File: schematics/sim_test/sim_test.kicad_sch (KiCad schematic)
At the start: 6 parts, among them U1 INA849D

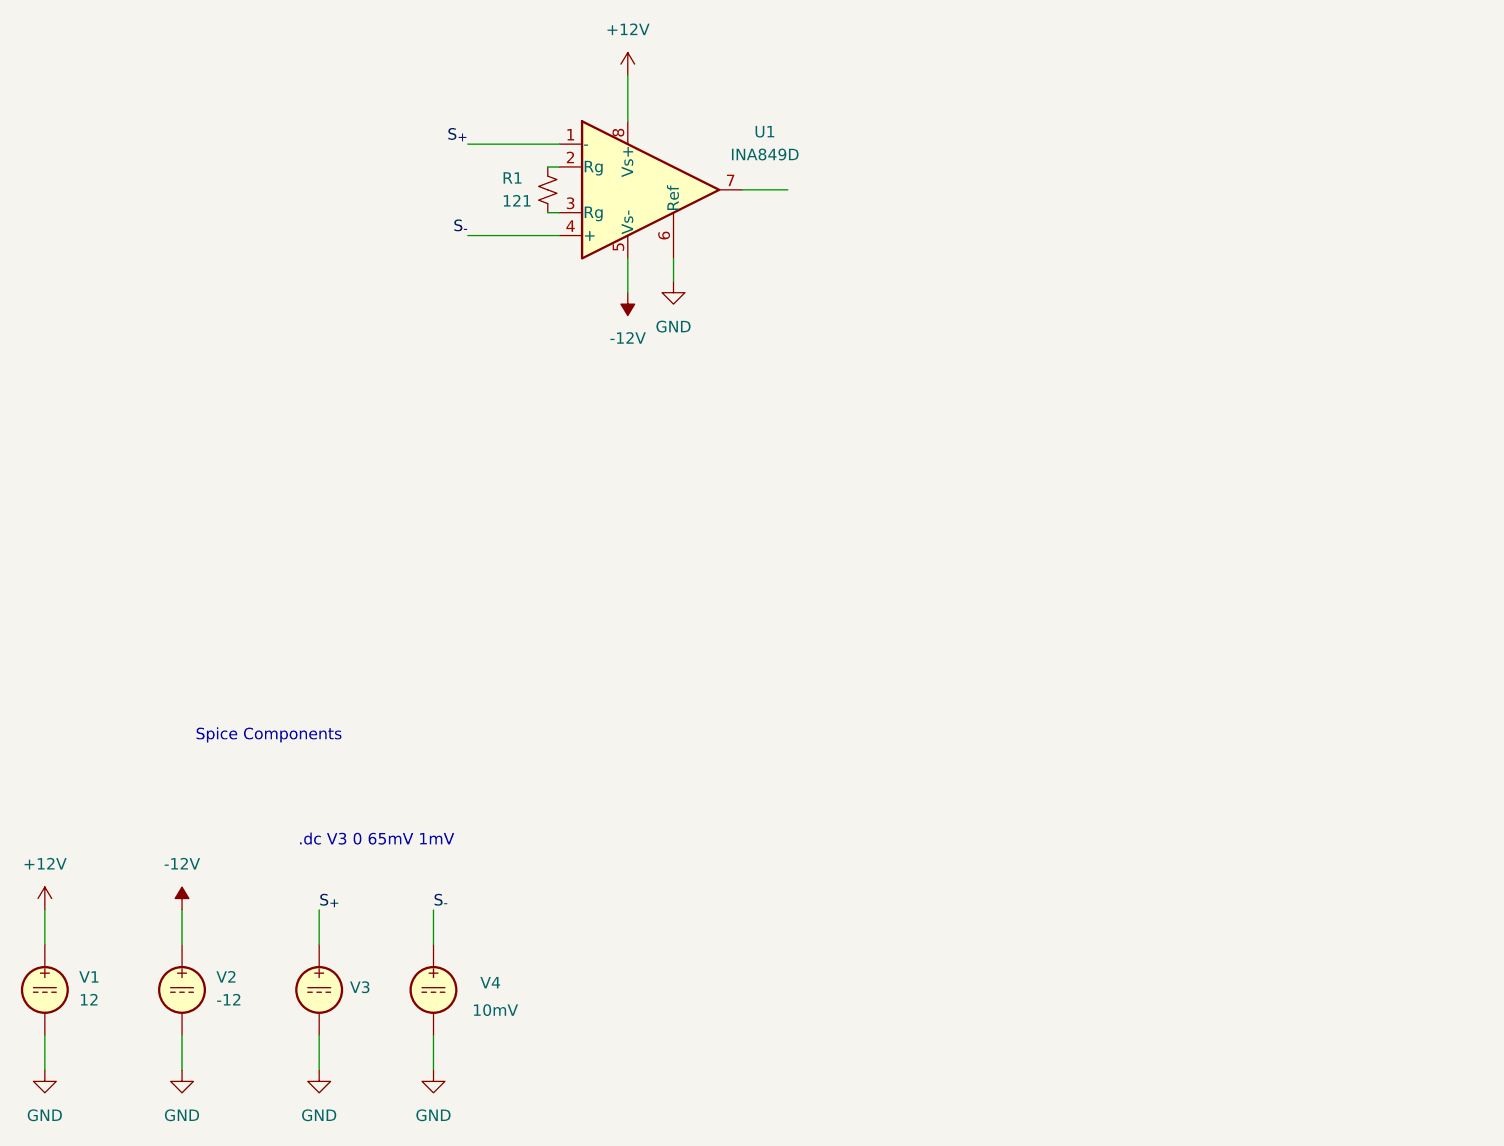
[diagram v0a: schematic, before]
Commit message: feat(sim): SG sig chain
Signed-off-by: Andrew Balmos <andrew@balmos.org>
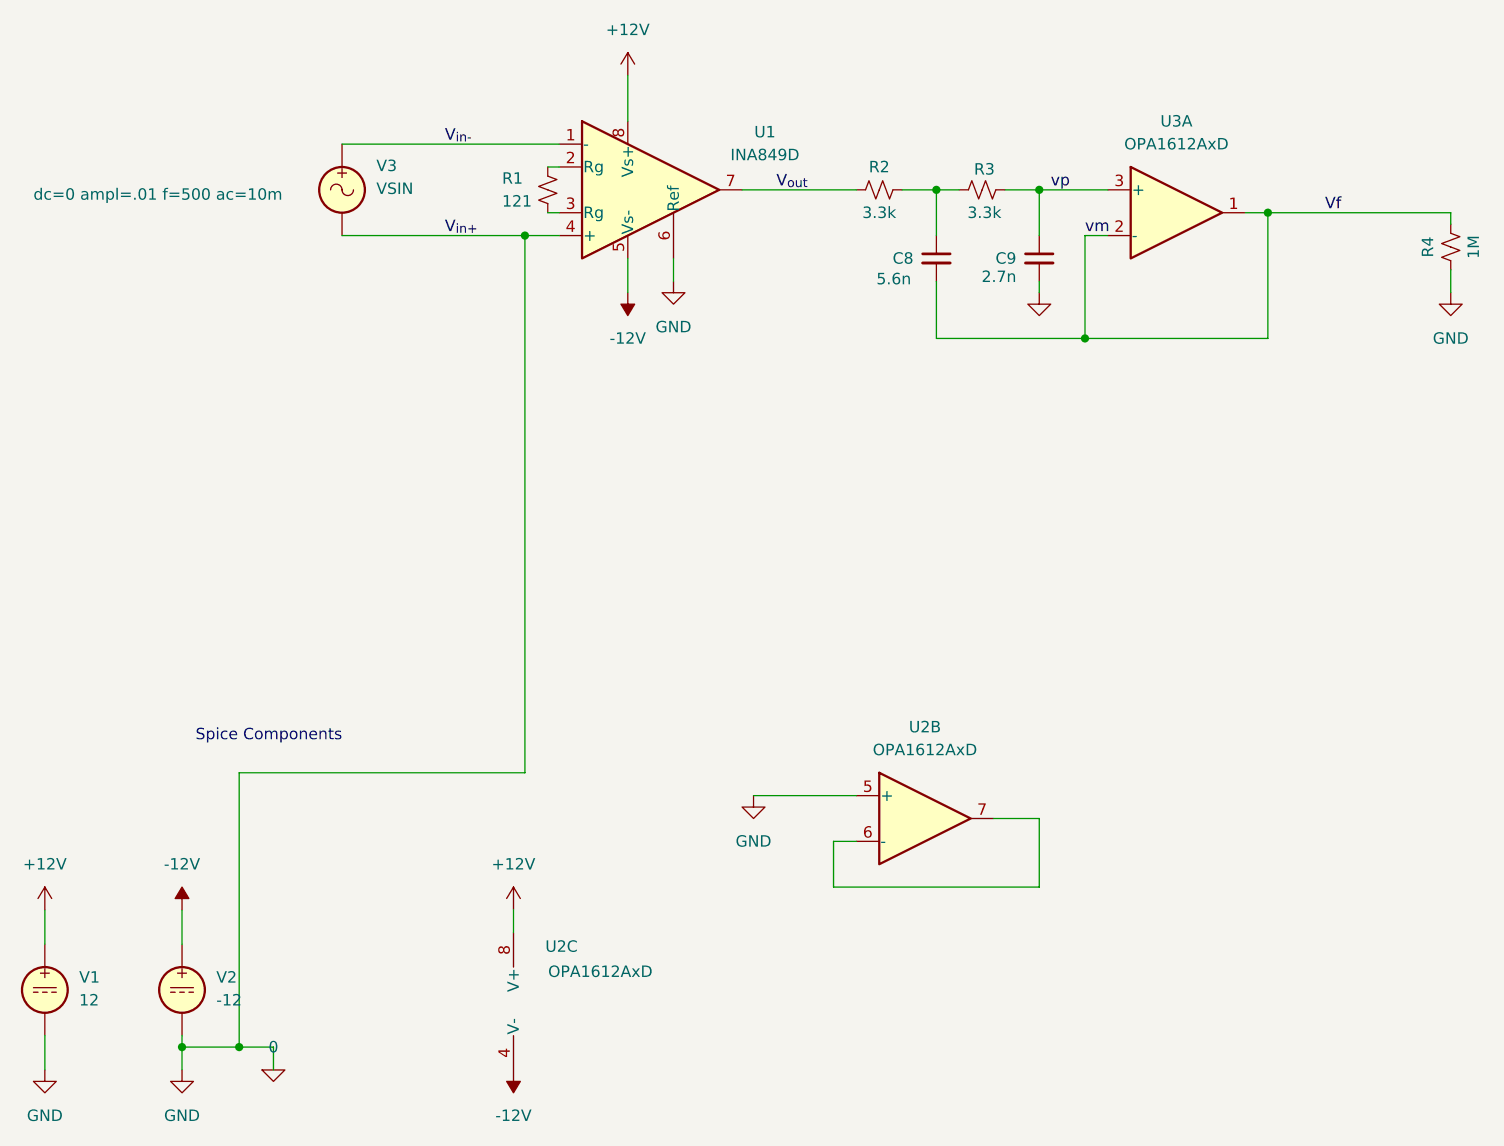
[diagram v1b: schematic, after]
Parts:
- removed V3: 1, symbol Simulation_SPICE:VDC
- removed V4: 10mV, symbol Simulation_SPICE:VDC
- added C8: 5.6n, Capacitor_SMD:C_0402_1005Metric, symbol Device:C_Small
- added C9: 2.7n, Capacitor_SMD:C_0402_1005Metric, symbol Device:C_Small
- added R2, R3: 3.3k, Resistor_SMD:R_0603_1608Metric, symbol Device:R_Small_US
- added R4: 1M, Resistor_SMD:R_0603_1608Metric, symbol Device:R_Small_US
- added U2, U3: OPA1612AxD, Link_Footprints:OPA1612, symbol Amplifier_Operational:OPA1612AxD
- added V3: VSIN, symbol Simulation_SPICE:VSIN
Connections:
- net S_{-} is gone; now on net 0: U1.4 (+)
- net +12V: now also U2.8 (V+)
- net -12V: now also U2.4 (V-)
- net V_{out}: now reaches U1.7
- net V_{out}: now also R2.1
- net GND renamed 0
- net 0: now also C9.2, R4.1, U2.5 (+), V3.2
- net S_{+} renamed V_{in-}
- net V_{in-}: now also V3.1
- new net: C8.1, R2.2, R3.1
- new net: U2.6 (-), U2.7
- new net Vf: C8.2, R4.2, U3.1, U3.2 (-)
- new net vp: C9.1, R3.2, U3.3 (+)
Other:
- note removed: ".dc V3 0 65mV 1mV"

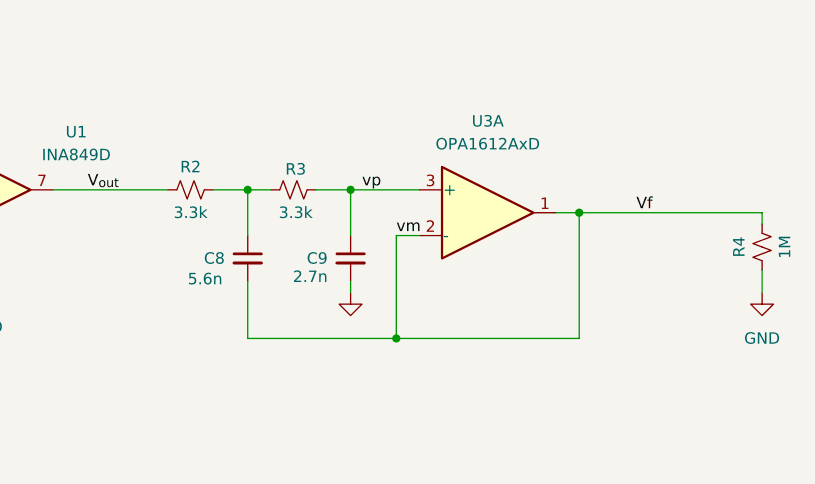
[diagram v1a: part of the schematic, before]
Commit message: bug(sg): Fix sim config
Signed-off-by: Andrew Balmos <andrew@balmos.org>
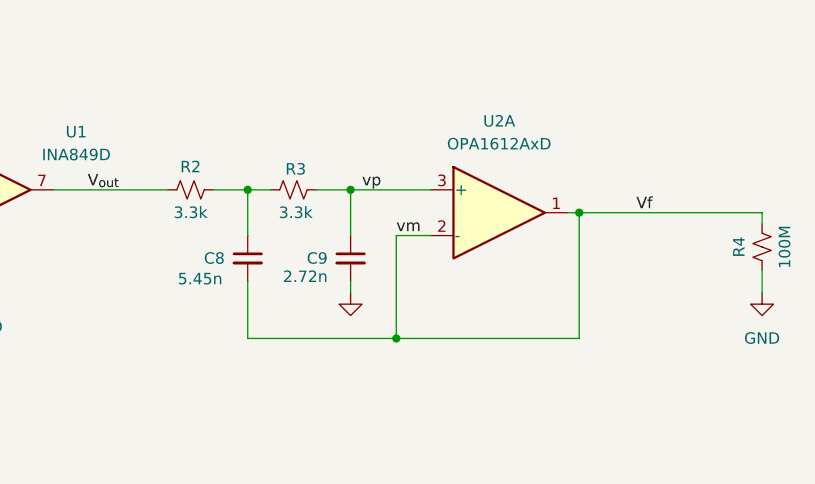
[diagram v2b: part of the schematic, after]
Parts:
- C8: value 5.6n -> 5.45n
- C9: value 2.7n -> 2.72n
- R4: value 1M -> 100M
- renumbered U3 to U2
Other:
- moved on the sheet: U2A

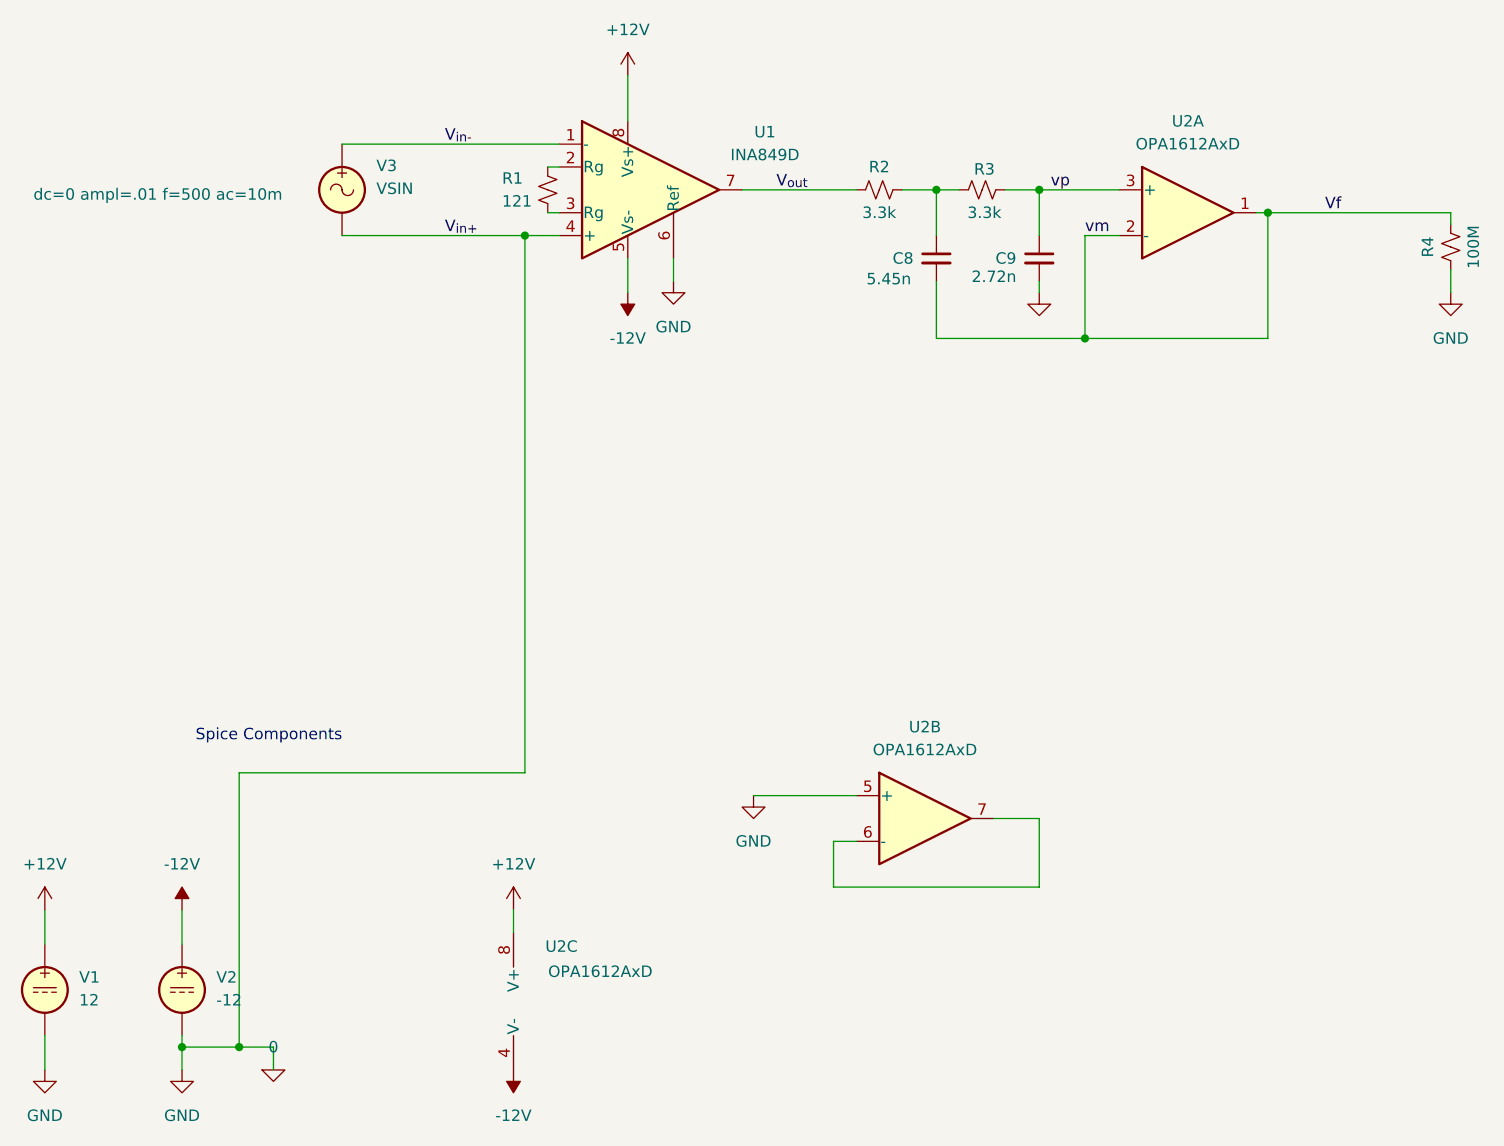
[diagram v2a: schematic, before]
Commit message: bug(sg): remove extra ground wire
Signed-off-by: Andrew Balmos <andrew@balmos.org>
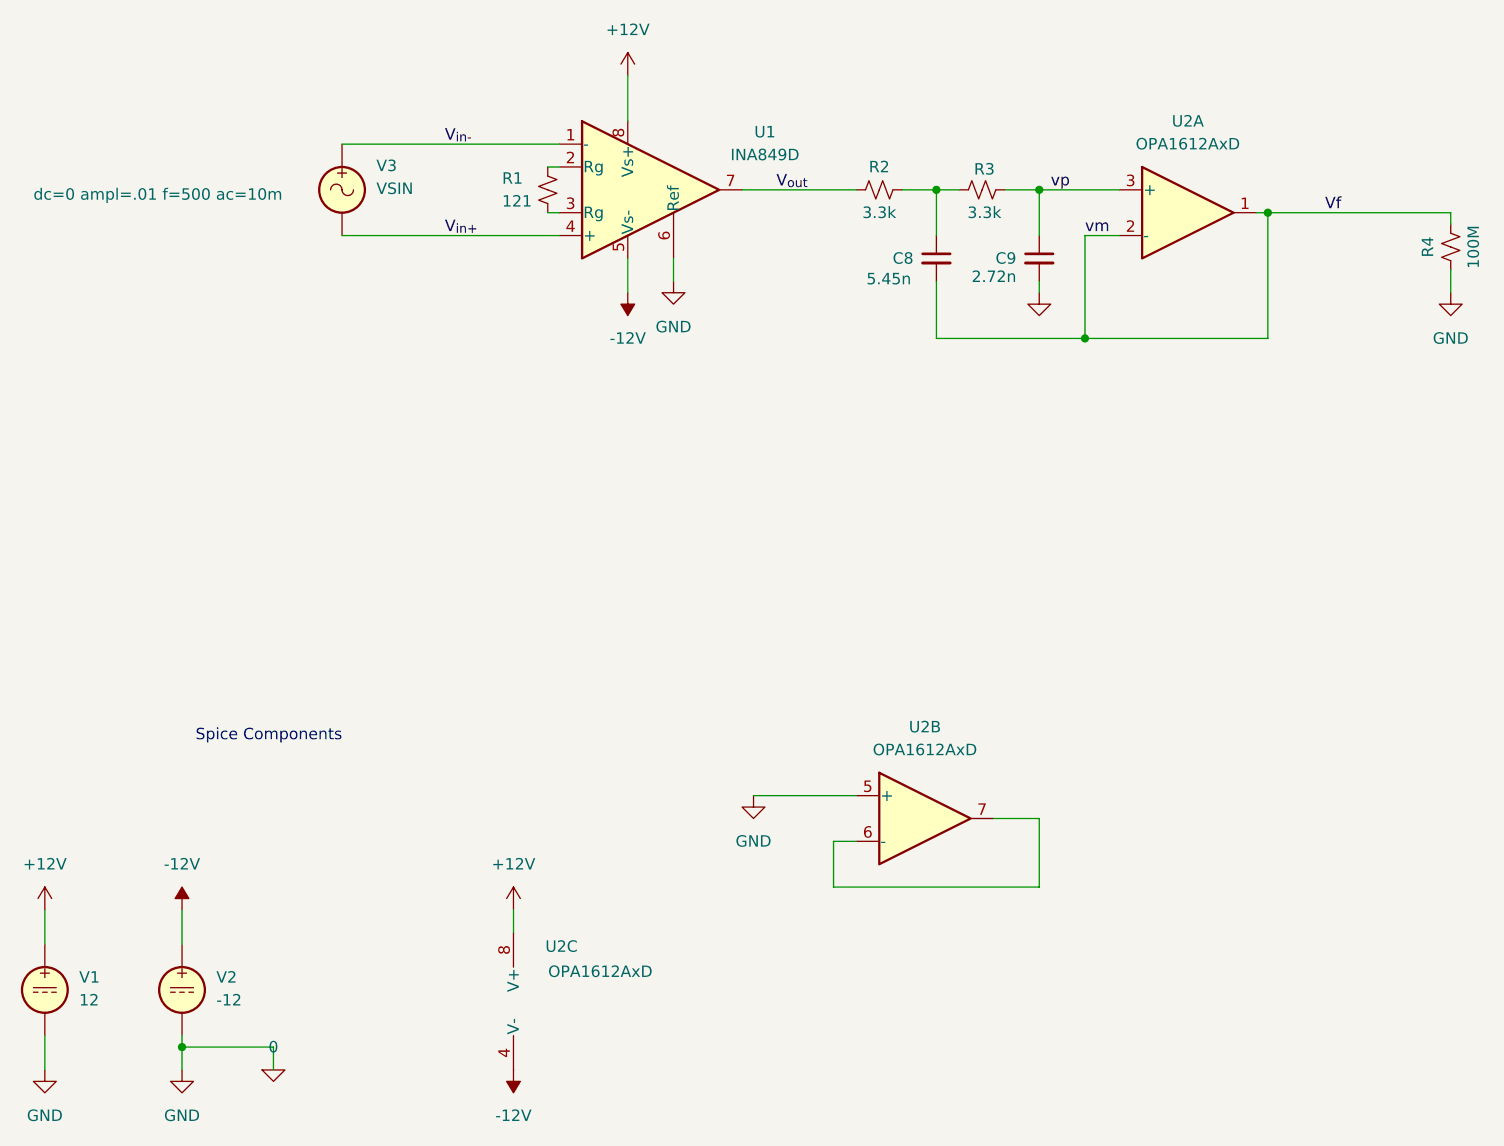
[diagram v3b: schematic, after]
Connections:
- net 0: no longer U1.4 (+), V3.2
- new net V_{in+}: U1.4 (+), V3.2
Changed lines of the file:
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@@
-	)
-	(junction
-		(at 64.77 157.48)
-		(diameter 0)
-		(color 0 0 0 0)
 	)
 	(junction
@@
 	)
 	(junction
-		(at 96.52 67.31)
-		(diameter 0)
-		(color 0 0 0 0)
-	)
-	(junction
 		(at 158.75 78.74)
 		(diameter 0)
@@
 	(wire
 		(pts
-			(xy 96.52 67.31) (xy 96.52 127)
-		)
-		(stroke
-			(width 0)
-			(type default)
-		)
-	)
-	(wire
-		(pts
 			(xy 179.07 64.77) (xy 179.07 78.74)
 		)
@@
 	(wire
 		(pts
-			(xy 64.77 127) (xy 64.77 157.48)
-		)
-		(stroke
-			(width 0)
-			(type default)
-		)
-	)
-	(wire
-		(pts
 			(xy 153.67 72.39) (xy 153.67 73.66)
 		)
@@
 	(wire
 		(pts
-			(xy 96.52 127) (xy 64.77 127)
-		)
-		(stroke
-			(width 0)
-			(type default)
-		)
-	)
-	(wire
-		(pts
 			(xy 95.25 142.24) (xy 95.25 144.78)
 		)
@@
 	(wire
 		(pts
-			(xy 68.58 157.48) (xy 64.77 157.48)
+			(xy 58.42 157.48) (xy 68.58 157.48)
 		)
 		(stroke
@@
 	(wire
 		(pts
-			(xy 76.2 67.31) (xy 96.52 67.31)
+			(xy 76.2 67.31) (xy 100.33 67.31)
 		)
 		(stroke
@@
 	(wire
 		(pts
-			(xy 64.77 157.48) (xy 58.42 157.48)
-		)
-		(stroke
-			(width 0)
-			(type default)
-		)
-	)
-	(wire
-		(pts
 			(xy 158.75 78.74) (xy 179.07 78.74)
 		)
@@
 		)
 		(stroke
-			(width 0)
-			(type default)
-		)
-	)
-	(wire
-		(pts
-			(xy 96.52 67.31) (xy 100.33 67.31)
-		)
-		(stroke
